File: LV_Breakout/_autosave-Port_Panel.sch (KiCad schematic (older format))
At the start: 36 parts, among them J1 171-009-113R911, J10 TE 776228-1, J11 2.54mmPins, J2 B3B-PH-K-S(LF)(SN), J3 Conn_02x03_Odd_Even, J4 171-009-213R001, J5 USB_B, J6 RJ45, J7 B6B-XH-A(LF)(SN), J8 B12B-PUDSS-1(LF)(SN)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

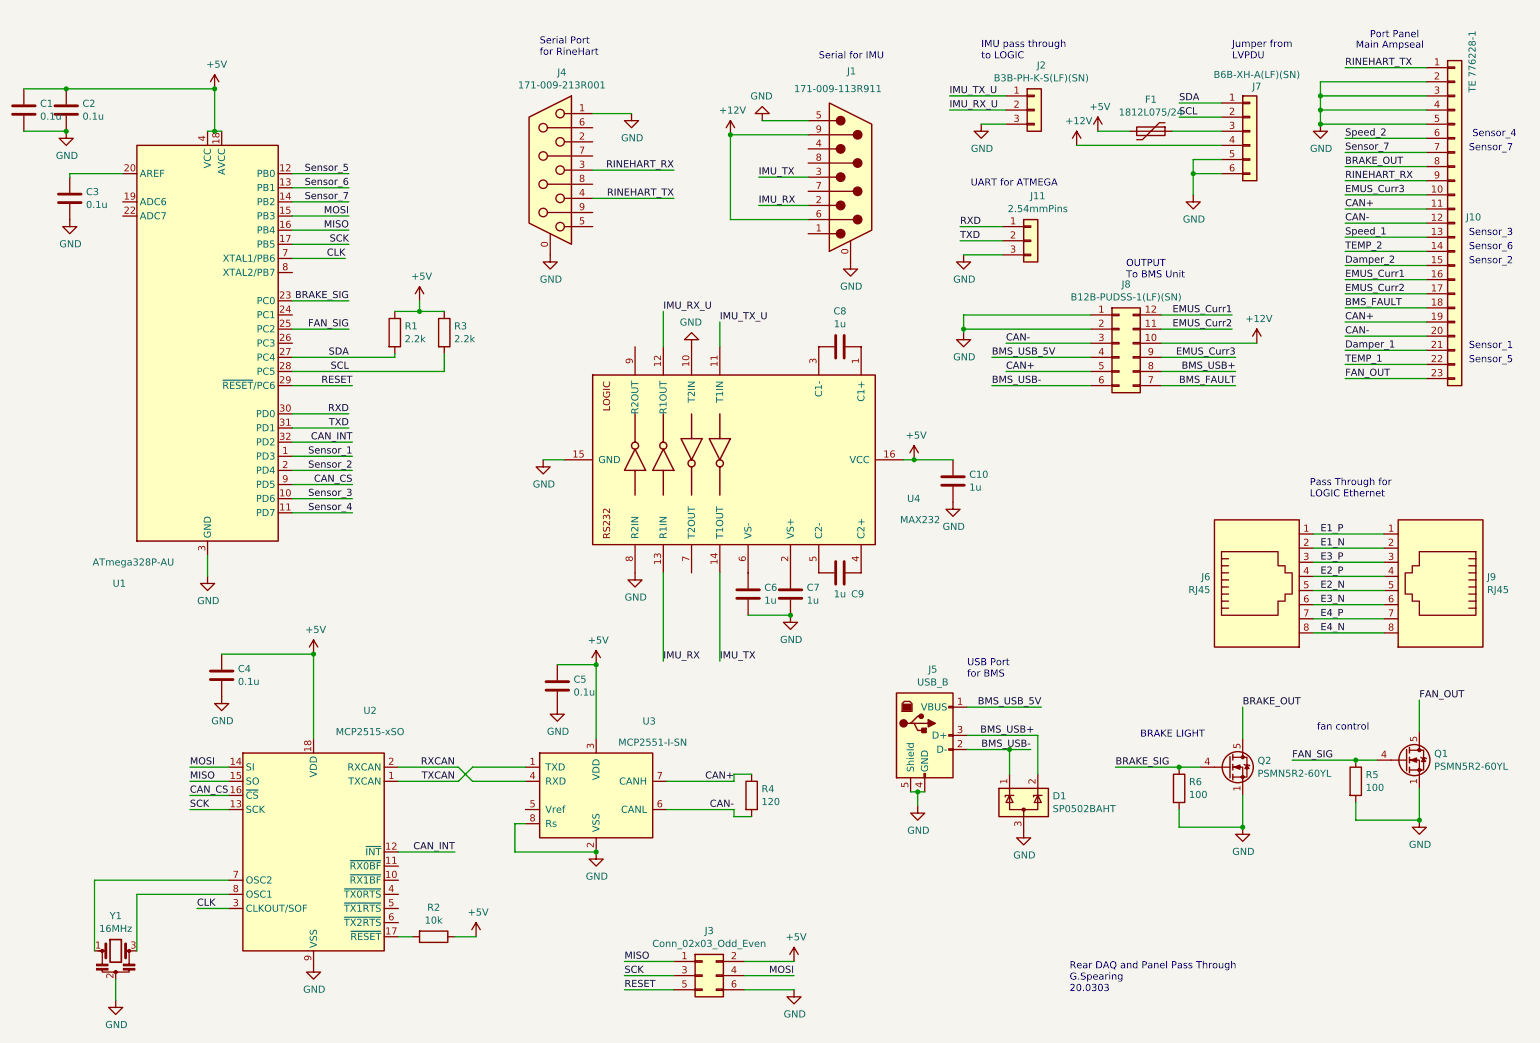
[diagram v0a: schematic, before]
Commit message: update code functionality per board
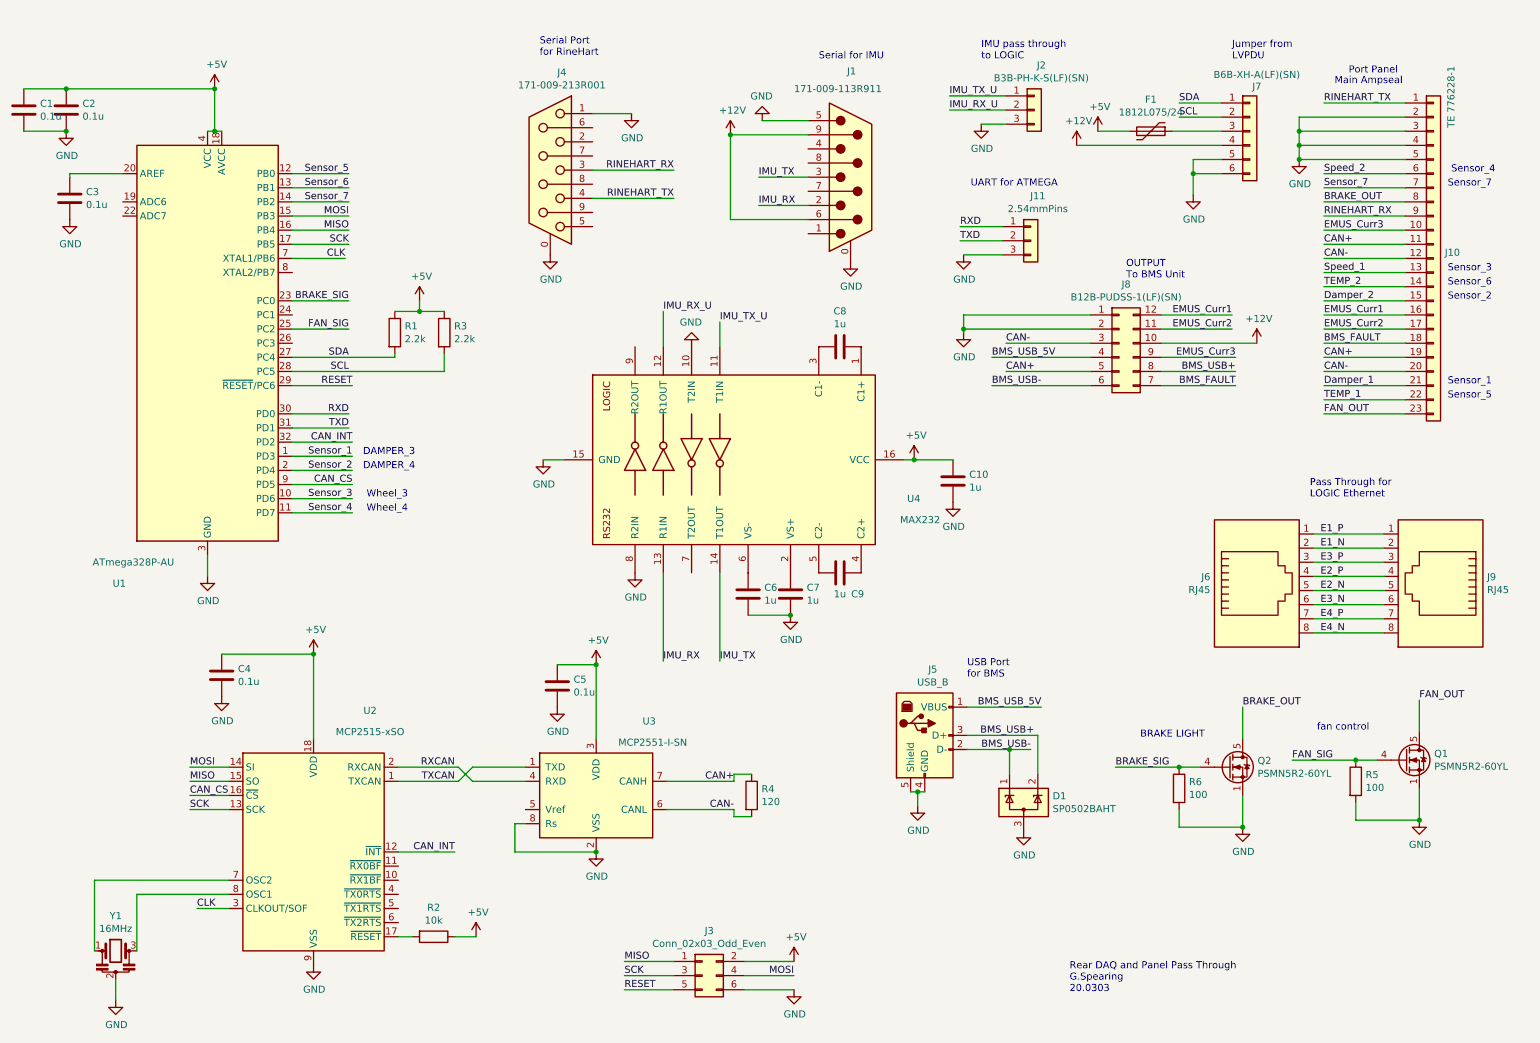
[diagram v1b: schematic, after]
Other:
- note added: "DAMPER_3"
- note added: "DAMPER_4\n"
- note added: "Wheel_3"
- note added: "Wheel_4"
- moved on the sheet: J10
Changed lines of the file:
@@
 L Connector_Generic:Conn_01x23 J10
 U 1 1 5E5779A1
-P 10825 1925
-F 0 "J10" H 10905 1967 50  0000 L CNN
-F 1 "TE 776228-1" V 10950 2850 50  0000 L CNN
-F 2 "AERO_CUSTOM:TE_1-776200-1_23pin_Vertical" H 10825 1925 50  0001 C CNN
-F 3 "~" H 10825 1925 50  0001 C CNN
-	1    10825 1925
+P 10675 2175
+F 0 "J10" H 10755 2217 50  0000 L CNN
+F 1 "TE 776228-1" V 10800 3100 50  0000 L CNN
+F 2 "AERO_CUSTOM:TE_1-776200-1_23pin_Vertical" H 10675 2175 50  0001 C CNN
+F 3 "~" H 10675 2175 50  0001 C CNN
+	1    10675 2175
 	1    0    0    -1
 $EndComp
@@
 	9425 2775 8750 2775
 Wire Wire Line
-	10050 2125 10625 2125
-Wire Wire Line
-	10050 2925 10625 2925
-Wire Wire Line
-	10050 1325 10625 1325
-Wire Wire Line
-	10050 2025 10625 2025
-Wire Wire Line
-	10625 2825 10050 2825
-Wire Wire Line
-	10625 2725 10050 2725
-Text Label 10050 2825 0    50   ~ 0
+	9900 2375 10475 2375
+Wire Wire Line
+	9900 3175 10475 3175
+Wire Wire Line
+	9900 1575 10475 1575
+Wire Wire Line
+	9900 2275 10475 2275
+Wire Wire Line
+	10475 3075 9900 3075
+Wire Wire Line
+	10475 2975 9900 2975
+Text Label 9900 3075 0    50   ~ 0
 Damper_1
-Text Label 10050 2225 0    50   ~ 0
+Text Label 9900 2475 0    50   ~ 0
 Damper_2
-Text Label 10050 2025 0    50   ~ 0
+Text Label 9900 2275 0    50   ~ 0
 Speed_1
-Text Label 10050 1325 0    50   ~ 0
+Text Label 9900 1575 0    50   ~ 0
 Speed_2
-Text Label 10050 2925 0    50   ~ 0
+Text Label 9900 3175 0    50   ~ 0
 TEMP_1
-Text Label 10050 2125 0    50   ~ 0
+Text Label 9900 2375 0    50   ~ 0
 TEMP_2
 Text Label 3000 2475 2    50   ~ 0
@@
 Sensor_7
 Wire Wire Line
-	10625 2225 10050 2225
-Text Label 10050 2625 0    50   ~ 0
+	10475 2475 9900 2475
+Text Label 9900 2875 0    50   ~ 0
 CAN+
 Wire Wire Line
-	10050 1425 10625 1425
-Wire Wire Line
-	10050 1525 10625 1525
-Wire Wire Line
-	10050 3025 10625 3025
-Text Label 10050 1525 0    50   ~ 0
+	9900 1675 10475 1675
+Wire Wire Line
+	9900 1775 10475 1775
+Wire Wire Line
+	9900 3275 10475 3275
+Text Label 9900 1775 0    50   ~ 0
 BRAKE_OUT
 Wire Wire Line
-	10050 2625 10625 2625
-Text Label 10050 2725 0    50   ~ 0
+	9900 2875 10475 2875
+Text Label 9900 2975 0    50   ~ 0
 CAN-
 Wire Wire Line
-	10050 1925 10625 1925
+	9900 2175 10475 2175
 $Comp
 L power:GND #PWR026
 U 1 1 5E62FDAB
-P 9875 1225
-F 0 "#PWR026" H 9875 975 50  0001 C CNN
-F 1 "GND" H 9880 1052 50  0000 C CNN
-F 2 "" H 9875 1225 50  0001 C CNN
-F 3 "" H 9875 1225 50  0001 C CNN
-	1    9875 1225
-	1    0    0    -1
-$EndComp
-Wire Wire Line
-	9875 1225 10625 1225
-Wire Wire Line
-	10625 1125 9875 1125
-Wire Wire Line
-	9875 1125 9875 1225
-Connection ~ 9875 1225
-Wire Wire Line
-	10625 1025 9875 1025
-Wire Wire Line
-	9875 1025 9875 1125
-Connection ~ 9875 1125
-Wire Wire Line
-	10625 925  9875 925
-Wire Wire Line
-	9875 925  9875 1025
-Connection ~ 9875 1025
-Text Label 10050 1625 0    50   ~ 0
+P 9725 1475
+F 0 "#PWR026" H 9725 1225 50  0001 C CNN
+F 1 "GND" H 9730 1302 50  0000 C CNN
+F 2 "" H 9725 1475 50  0001 C CNN
+F 3 "" H 9725 1475 50  0001 C CNN
+	1    9725 1475
+	1    0    0    -1
+$EndComp
+Wire Wire Line
+	9725 1475 10475 1475
+Wire Wire Line
+	10475 1375 9725 1375
+Wire Wire Line
+	9725 1375 9725 1475
+Connection ~ 9725 1475
+Wire Wire Line
+	10475 1275 9725 1275
+Wire Wire Line
+	9725 1275 9725 1375
+Connection ~ 9725 1375
+Wire Wire Line
+	10475 1175 9725 1175
+Wire Wire Line
+	9725 1175 9725 1275
+Connection ~ 9725 1275
+Text Label 9900 1875 0    50   ~ 0
 RINEHART_RX
 Wire Wire Line
-	10050 2425 10625 2425
-Text Label 10050 825  0    50   ~ 0
+	9900 2675 10475 2675
+Text Label 9900 1075 0    50   ~ 0
 RINEHART_TX
 Wire Wire Line
-	10050 2325 10625 2325
-Text Label 10050 2525 0    50   ~ 0
+	9900 2575 10475 2575
+Text Label 9900 2775 0    50   ~ 0
 BMS_FAULT
 Wire Wire Line
-	10050 1725 10625 1725
-Text Label 10050 1825 0    50   ~ 0
+	9900 1975 10475 1975
+Text Label 9900 2075 0    50   ~ 0
 CAN+
 Wire Wire Line
-	10050 2525 10625 2525
-Text Label 10050 1925 0    50   ~ 0
+	9900 2775 10475 2775
+Text Label 9900 2175 0    50   ~ 0
 CAN-
 Wire Wire Line
-	10050 1825 10625 1825
+	9900 2075 10475 2075
 $Comp
 L Connector_Generic:Conn_01x06 J7
@@
 Text Notes 4350 750  0    50   ~ 0
 Serial Port\nfor RineHart
-Text Notes 10125 700  0    50   ~ 0
+Text Notes 9975 950  0    50   ~ 0
 Main Ampseal
 Text Label 9250 2675 2    50   ~ 0
 EMUS_Curr2
-Text Label 10050 2325 0    50   ~ 0
+Text Label 9900 2575 0    50   ~ 0
 EMUS_Curr1
 Wire Wire Line
-	10625 1625 10050 1625
-Wire Wire Line
-	10625 825  10050 825
+	10475 1875 9900 1875
+Wire Wire Line
+	10475 1075 9900 1075
 $Comp
 L Device:R R1
@@
 Wire Wire Line
 	10575 5300 10575 5525
-Text Label 10050 3025 0    50   ~ 0
+Text Label 9900 3275 0    50   ~ 0
 FAN_OUT
 $Comp
@@
 	1    0    0    -1
 $EndComp
-Text Label 10050 1425 0    50   ~ 0
+Text Label 9900 1675 0    50   ~ 0
 Sensor_7
-Text Label 10050 2425 0    50   ~ 0
+Text Label 9900 2675 0    50   ~ 0
 EMUS_Curr2
 Text Label 9250 2575 2    50   ~ 0
 EMUS_Curr1
-Text Label 10050 1725 0    50   ~ 0
+Text Label 9900 1975 0    50   ~ 0
 EMUS_Curr3
 Text Label 9275 2875 2    50   ~ 0
@@
 Wire Wire Line
 	8150 1375 9175 1375
-Text Notes 10225 625  0    50   ~ 0
+Text Notes 10075 875  0    50   ~ 0
 Port Panel
 Text Notes 8600 5575 0    50   ~ 0
@@
 Text Notes 8100 7375 0    50   ~ 0
 Rear DAQ and Panel Pass Through\nG.Spearing\n20.0303
-Text Notes 10925 2925 0    50   ~ 0
+Text Notes 10775 3175 0    50   ~ 0
 Sensor_5\n
-Text Notes 10925 2825 0    50   ~ 0
+Text Notes 10775 3075 0    50   ~ 0
 Sensor_1\n
-Text Notes 10925 2025 0    50   ~ 0
+Text Notes 10775 2275 0    50   ~ 0
 Sensor_3
-Text Notes 10925 2125 0    50   ~ 0
+Text Notes 10775 2375 0    50   ~ 0
 Sensor_6
-Text Notes 10925 2225 0    50   ~ 0
+Text Notes 10775 2475 0    50   ~ 0
 Sensor_2\n
-Text Notes 10925 1425 0    50   ~ 0
+Text Notes 10775 1675 0    50   ~ 0
 Sensor_7\n
-Text Notes 10950 1325 0    50   ~ 0
+Text Notes 10800 1575 0    50   ~ 0
 Sensor_4
+Text Notes 3100 3575 0    50   ~ 0
+DAMPER_3
+Text Notes 3100 3675 0    50   ~ 0
+DAMPER_4\n
+Text Notes 3125 3875 0    50   ~ 0
+Wheel_3
+Text Notes 3125 3975 0    50   ~ 0
+Wheel_4
 $EndSCHEMATC
